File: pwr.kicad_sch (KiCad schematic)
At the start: 7 parts

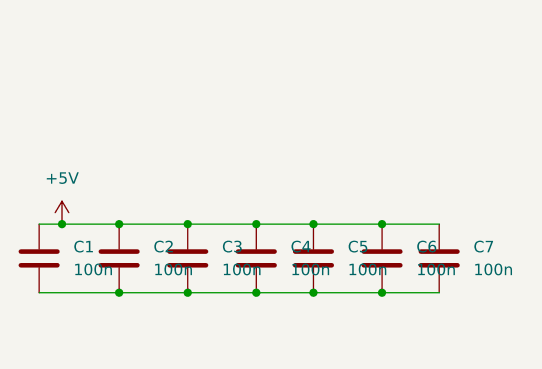
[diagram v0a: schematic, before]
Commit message: Remove all GND hierarchical pins and labels from all sheets
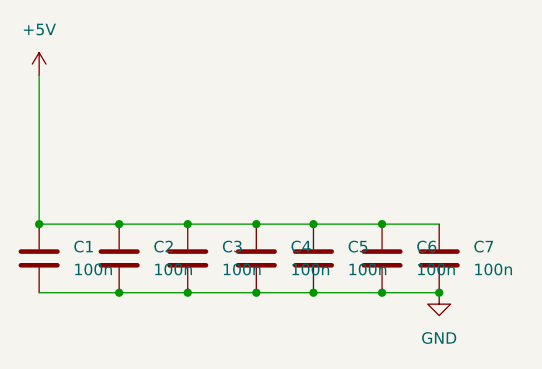
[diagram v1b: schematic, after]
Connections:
- net GND: now reaches C1.2, C2.2, C3.2, C4.2, C5.2, C6.2, C7.2
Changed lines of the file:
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@@
+	)
+	(junction
+		(at 153.67 107.95)
+		(diameter 0)
+		(color 0 0 0 0)
 	)
 	(junction
@@
 	)
 	(junction
+		(at 109.22 100.33)
+		(diameter 0)
+		(color 0 0 0 0)
+	)
+	(junction
 		(at 139.7 107.95)
 		(diameter 0)
@@
 	)
 	(junction
-		(at 111.76 100.33)
-		(diameter 0)
-		(color 0 0 0 0)
-	)
-	(junction
 		(at 118.11 100.33)
 		(diameter 0)
@@
 	(wire
 		(pts
-			(xy 109.22 100.33) (xy 111.76 100.33)
+			(xy 109.22 83.82) (xy 109.22 100.33)
+		)
+		(stroke
+			(width 0)
+			(type default)
+		)
+	)
+	(wire
+		(pts
+			(xy 109.22 100.33) (xy 118.11 100.33)
 		)
 		(stroke
@@
 		(pts
 			(xy 125.73 107.95) (xy 133.35 107.95)
-		)
-		(stroke
-			(width 0)
-			(type default)
-		)
-	)
-	(wire
-		(pts
-			(xy 111.76 100.33) (xy 118.11 100.33)
 		)
 		(stroke
@@
 	(symbol
 		(lib_id "power:+5V")
-		(at 111.76 100.33 0)
+		(at 109.22 83.82 0)
 		(unit 1)
 		(body_style 1)
@@
 		(fields_autoplaced yes)
 		(property "Reference" "#PWR04"
-			(at 111.76 104.14 0)
+			(at 109.22 87.63 0)
 			(hide yes)
 			(show_name no)
@@
 		)
 		(property "Value" "+5V"
-			(at 111.76 95.25 0)
+			(at 109.22 78.74 0)
 			(show_name no)
 			(do_not_autoplace no)
@@
 		)
 		(property "Footprint" ""
-			(at 111.76 100.33 0)
+			(at 109.22 83.82 0)
 			(hide yes)
 			(show_name no)
@@
 		)
 		(property "Datasheet" ""
-			(at 111.76 100.33 0)
+			(at 109.22 83.82 0)
 			(hide yes)
 			(show_name no)
@@
 		)
 		(property "Description" ""
-			(at 111.76 100.33 0)
+			(at 109.22 83.82 0)
 			(show_name no)
 			(do_not_autoplace no)
@@
 					(unit 1)
 				)
+			)
+		)
+	)
+	(symbol
+		(lib_id "power:GND")
+		(at 153.67 107.95 0)
+		(unit 1)
+		(body_style 1)
+		(exclude_from_sim no)
+		(in_bom yes)
+		(on_board yes)
+		(in_pos_files yes)
+		(dnp no)
+		(fields_autoplaced yes)
+		(property "Reference" "#PWR022"
+			(at 153.67 114.3 0)
+			(hide yes)
+			(show_name no)
+			(do_not_autoplace no)
+			(effects
+				(font
+					(size 1.27 1.27)
+				)
+			)
+		)
+		(property "Value" "GND"
+			(at 153.67 113.03 0)
+			(show_name no)
+			(do_not_autoplace no)
+			(effects
+				(font
+					(size 1.27 1.27)
+				)
+			)
+		)
+		(property "Footprint" ""
+			(at 153.67 107.95 0)
+			(hide yes)
+			(show_name no)
+			(do_not_autoplace no)
+			(effects
+				(font
+					(size 1.27 1.27)
+				)
+			)
+		)
+		(property "Datasheet" ""
+			(at 153.67 107.95 0)
+			(hide yes)
+			(show_name no)
+			(do_not_autoplace no)
+			(effects
+				(font
+					(size 1.27 1.27)
+				)
+			)
+		)
+		(property "Description" ""
+			(at 153.67 107.95 0)
+			(show_name no)
+			(do_not_autoplace no)
+			(effects
+				(font
+					(size 1.27 1.27)
+				)
+			)
+		)
+		(pin "1"
+		)
+		(instances
+			(project "nfc_rpi"
+				(path "/49150dc2-d01c-4907-8daf-0ff812da3f6d/05894123-5cc5-4ad3-b976-a2cb5434e1fc/195d9f98-a83f-43b9-8312-c38d1e087b70"
+					(reference "#PWR022")
+					(unit 1)
+				)

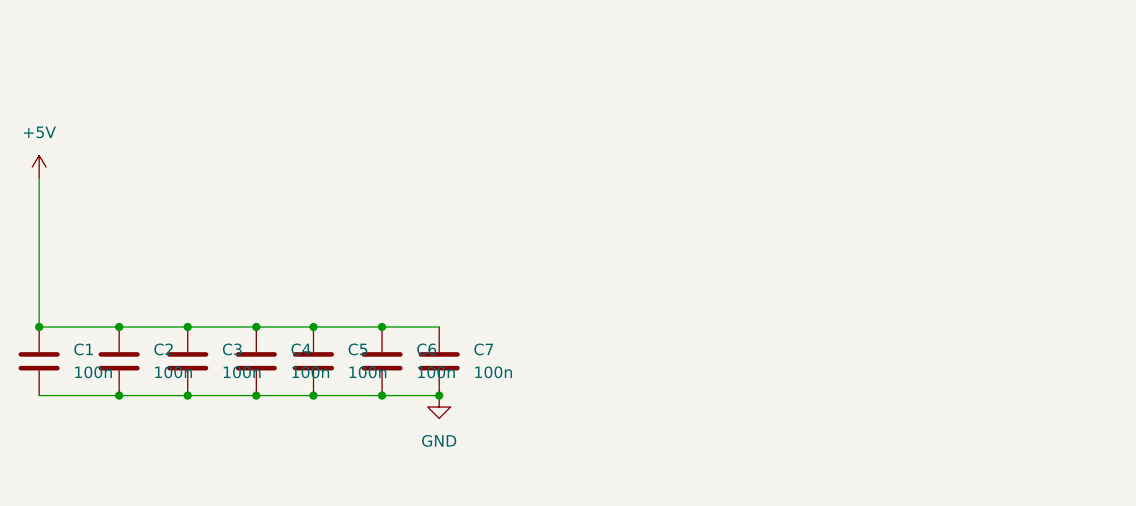
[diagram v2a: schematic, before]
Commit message: Add hierarchical labels/pins across all sheets, fix DiscoveryAnalog3 rename, PCB 99x99mm rounded corners
- nfc_rpi.kicad_sch: 19 hierarchical pins on PN532 sheet
- pn532.kicad_sch: 22 hierarchical labels with _PN532 suffix
- raspberry_pn532.kicad_sch: 68 hierarchical labels for J1
- nfc.kicad_sch: 54 signal pins on Raspberry sheet, power pins removed
- switch.kicad_sch: 8 switch+resistor circuits with hierarchical labels
- oled.kicad_sch: 7 hierarchical labels
- DiscoveryAnalog3.kicad_sch: 26 hierarchical labels for J4 connector
- nfc_rpi.kicad_pcb: 99x99mm board outline with 5mm rounded corners (gr_line + gr_arc)
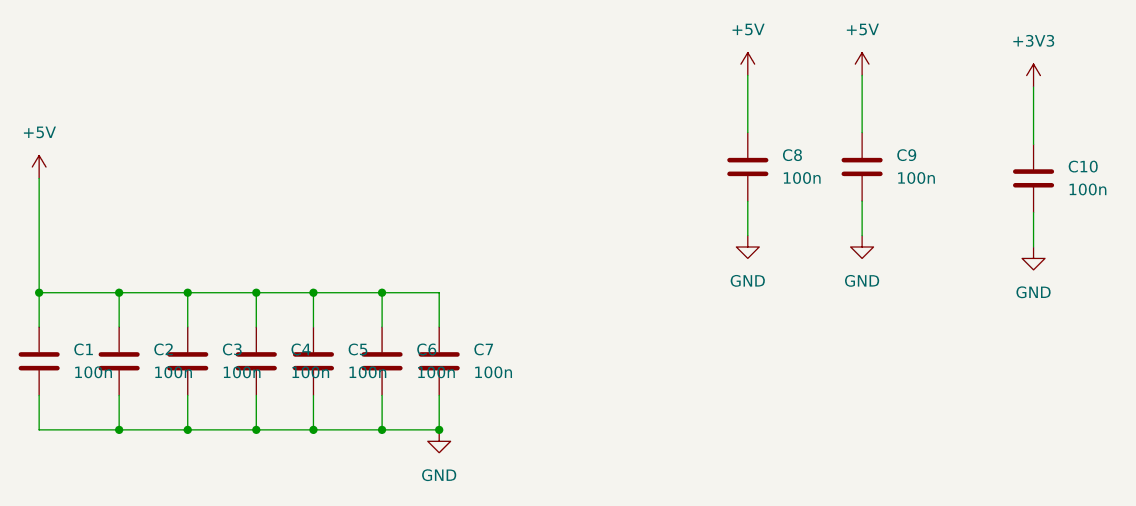
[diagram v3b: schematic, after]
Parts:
- added C10, C8, C9: 100n, Capacitor_SMD:C_0603_1608Metric, symbol Device:C
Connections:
- net +5V: now also C8.1, C9.1
- net GND: now also C10.2, C8.2, C9.2
- new net +3V3: C10.1
